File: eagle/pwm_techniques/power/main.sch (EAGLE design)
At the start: 12 parts

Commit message: [ update ] pwm_techniques/power
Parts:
- added C7: 15u, rcl:C-EUC1206
- added L1: 33u, rcl:L-EUTJ3-U2
- added LOAD_CON: (no value), pinhead:PINHD-1X2
- added Q1, Q2, Q3, Q4: IRFP460A, irfp460a:IRFP460A
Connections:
- new net LOAD_N: LOAD_CON.2
- new net LOAD_P: LOAD_CON.1
- new net N$3: L1.2, Q1.SOURCE, Q3.DRAIN
- new net N$4: C7.1, L1.1
- new net N$5: C7.2, Q2.SOURCE, Q4.DRAIN
- net GND: now also Q3.SOURCE, Q4.SOURCE
- net PWR_170V: now also Q1.DRAIN, Q2.DRAIN
- net Q0_GATE: now also Q1.GATE
- net Q1_GATE: now also Q3.GATE
- net Q2_GATE: now also Q2.GATE
- net Q3_GATE: now also Q4.GATE
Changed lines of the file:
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@@
 <part name="C6" library="rcl" deviceset="C-EU" device="C1206" value="100n"/>
 <part name="PWR_CON" library="pinhead" deviceset="PINHD-1X2" device=""/>
+<part name="Q1" library="irfp460a" deviceset="IRFP460A" device=""/>
+<part name="Q2" library="irfp460a" deviceset="IRFP460A" device=""/>
+<part name="Q3" library="irfp460a" deviceset="IRFP460A" device=""/>
+<part name="Q4" library="irfp460a" deviceset="IRFP460A" device=""/>
+<part name="L1" library="rcl" deviceset="L-EU" device="TJ3-U2" value="33u"/>
+<part name="C7" library="rcl" deviceset="C-EU" device="C1206" value="15u"/>
+<part name="LOAD_CON" library="pinhead" deviceset="PINHD-1X2" device=""/>
 </parts>
 <sheets>
@@
 <instance part="C6" gate="G$1" x="-7.62" y="-20.32"/>
 <instance part="PWR_CON" gate="G$1" x="-40.64" y="-5.08"/>
+<instance part="Q1" gate="G$1" x="106.68" y="22.86"/>
+<instance part="Q2" gate="G$1" x="160.02" y="22.86"/>
+<instance part="Q3" gate="G$1" x="106.68" y="-7.62"/>
+<instance part="Q4" gate="G$1" x="160.02" y="-7.62"/>
+<instance part="L1" gate="G$1" x="121.92" y="7.62" rot="R270"/>
+<instance part="C7" gate="G$1" x="134.62" y="7.62" rot="R90"/>
+<instance part="LOAD_CON" gate="G$1" x="-40.64" y="-22.86"/>
 </instances>
 <busses>
@@
 <label x="-68.58" y="-5.08" size="1.778" layer="95"/>
 </segment>
+<segment>
+<pinref part="Q3" gate="G$1" pin="SOURCE"/>
+<wire x1="93.98" y1="-12.7" x2="78.74" y2="-12.7" width="0.1524" layer="91"/>
+<label x="78.74" y="-12.7" size="1.778" layer="95"/>
+</segment>
+<segment>
+<pinref part="Q4" gate="G$1" pin="SOURCE"/>
+<wire x1="147.32" y1="-12.7" x2="127" y2="-12.7" width="0.1524" layer="91"/>
+<label x="127" y="-12.7" size="1.778" layer="95"/>
+</segment>
 </net>
 <net name="PWM_CTL_LO_0" class="0">
@@
 <label x="27.94" y="22.86" size="1.778" layer="95"/>
 </segment>
+<segment>
+<pinref part="Q1" gate="G$1" pin="GATE"/>
+<wire x1="93.98" y1="27.94" x2="78.74" y2="27.94" width="0.1524" layer="91"/>
+<label x="78.74" y="27.94" size="1.778" layer="95"/>
+</segment>
 </net>
 <net name="Q1_GATE" class="0">
@@
 <wire x1="25.4" y1="17.78" x2="38.1" y2="17.78" width="0.1524" layer="91"/>
 <label x="27.94" y="17.78" size="1.778" layer="95"/>
+</segment>
+<segment>
+<pinref part="Q3" gate="G$1" pin="GATE"/>
+<wire x1="93.98" y1="-2.54" x2="78.74" y2="-2.54" width="0.1524" layer="91"/>
+<label x="78.74" y="-2.54" size="1.778" layer="95"/>
 </segment>
 </net>
@@
 <label x="27.94" y="-12.7" size="1.778" layer="95"/>
 </segment>
+<segment>
+<pinref part="Q2" gate="G$1" pin="GATE"/>
+<wire x1="147.32" y1="27.94" x2="132.08" y2="27.94" width="0.1524" layer="91"/>
+<label x="132.08" y="27.94" size="1.778" layer="95"/>
+</segment>
 </net>
 <net name="Q3_GATE" class="0">
@@
 <label x="27.94" y="-17.78" size="1.778" layer="95"/>
 </segment>
+<segment>
+<pinref part="Q4" gate="G$1" pin="GATE"/>
+<wire x1="147.32" y1="-2.54" x2="127" y2="-2.54" width="0.1524" layer="91"/>
+<label x="127" y="-2.54" size="1.778" layer="95"/>
+</segment>
 </net>
 <net name="PWR_170V" class="0">
@@
 <label x="-68.58" y="-2.54" size="1.778" layer="95"/>
 </segment>
-</net>
+<segment>
+<pinref part="Q1" gate="G$1" pin="DRAIN"/>
+<wire x1="93.98" y1="22.86" x2="78.74" y2="22.86" width="0.1524" layer="91"/>
+<label x="78.74" y="22.86" size="1.778" layer="95"/>
+</segment>
+<segment>
+<pinref part="Q2" gate="G$1" pin="DRAIN"/>
+<wire x1="132.08" y1="22.86" x2="147.32" y2="22.86" width="0.1524" layer="91"/>
+<label x="132.08" y="22.86" size="1.778" layer="95"/>
+</segment>
+</net>
+<net name="N$3" class="0">
+<segment>
+<pinref part="Q1" gate="G$1" pin="SOURCE"/>
+<wire x1="93.98" y1="17.78" x2="91.44" y2="17.78" width="0.1524" layer="91"/>
+<wire x1="91.44" y1="17.78" x2="91.44" y2="7.62" width="0.1524" layer="91"/>
+<pinref part="L1" gate="G$1" pin="2"/>
+<wire x1="91.44" y1="7.62" x2="116.84" y2="7.62" width="0.1524" layer="91"/>
+<pinref part="Q3" gate="G$1" pin="DRAIN"/>
+<wire x1="93.98" y1="-7.62" x2="91.44" y2="-7.62" width="0.1524" layer="91"/>
+<wire x1="91.44" y1="-7.62" x2="91.44" y2="7.62" width="0.1524" layer="91"/>
+<junction x="91.44" y="7.62"/>
+</segment>
+</net>
+<net name="N$4" class="0">
+<segment>
+<pinref part="L1" gate="G$1" pin="1"/>
+<pinref part="C7" gate="G$1" pin="1"/>
+<wire x1="127" y1="7.62" x2="132.08" y2="7.62" width="0.1524" layer="91"/>
+</segment>
+</net>
+<net name="N$5" class="0">
+<segment>
+<pinref part="C7" gate="G$1" pin="2"/>
+<wire x1="139.7" y1="7.62" x2="144.78" y2="7.62" width="0.1524" layer="91"/>
+<wire x1="144.78" y1="7.62" x2="144.78" y2="17.78" width="0.1524" layer="91"/>
+<pinref part="Q2" gate="G$1" pin="SOURCE"/>
+<wire x1="144.78" y1="17.78" x2="147.32" y2="17.78" width="0.1524" layer="91"/>
+<pinref part="Q4" gate="G$1" pin="DRAIN"/>
+<wire x1="147.32" y1="-7.62" x2="144.78" y2="-7.62" width="0.1524" layer="91"/>
+<wire x1="144.78" y1="-7.62" x2="144.78" y2="7.62" width="0.1524" layer="91"/>
+<junction x="144.78" y="7.62"/>
+</segment>
+</net>
+<net name="LOAD_P" class="0">
+<segment>
+<pinref part="LOAD_CON" gate="G$1" pin="1"/>
+<wire x1="-43.18" y1="-20.32" x2="-68.58" y2="-20.32" width="0.1524" layer="91"/>
+<label x="-68.58" y="-20.32" size="1.778" layer="95"/>
+</segment>
+</net>
+<net name="LOAD_N" class="0">
+<segment>
+<pinref part="LOAD_CON" gate="G$1" pin="2"/>
+<wire x1="-43.18" y1="-22.86" x2="-68.58" y2="-22.86" width="0.1524" layer="91"/>
+<label x="-68.58" y="-22.86" size="1.778" layer="95"/>
+</segment>
+</net>

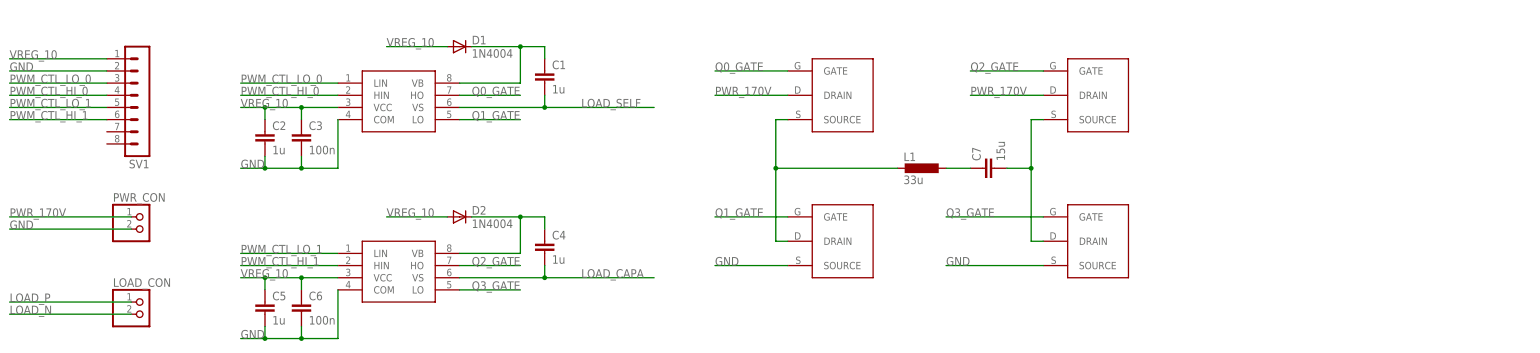
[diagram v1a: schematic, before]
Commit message: [ update ] add pwm exclusion logic
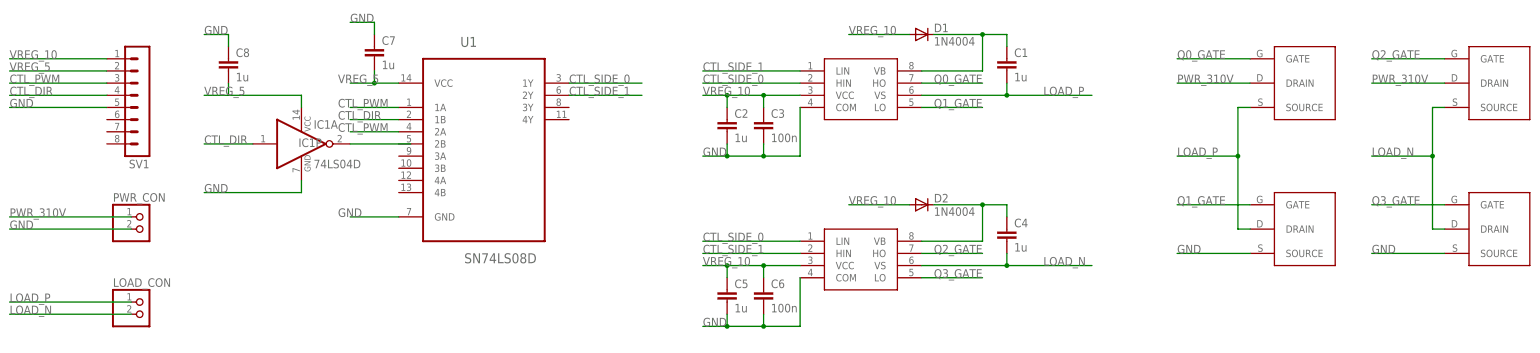
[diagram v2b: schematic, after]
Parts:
- removed L1: 33u, rcl:L-EUTJ3-U2
- added C8: 1u, rcl:C-EUC1206
- added IC1: 74LS04D, 74xx-eu:74LS04D
- added U1: SN74LS08D, sn74ls08d:SN74LS08D
- C7: value 15u -> 1u
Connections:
- net PWR_170V renamed PWR_310V
- removed net LOAD_CAPA: C4.2, IR2304_1.VS
- removed net LOAD_SELF: C1.2, IR2304_0.VS
- removed net N$3: L1.2, Q1.SOURCE, Q3.DRAIN
- removed net N$4: C7.1, L1.1
- removed net PWM_CTL_HI_0: IR2304_0.HIN, SV1.4
- removed net PWM_CTL_HI_1: IR2304_1.HIN, SV1.6
- removed net PWM_CTL_LO_0: IR2304_0.LIN, SV1.3
- removed net PWM_CTL_LO_1: IR2304_1.LIN, SV1.5
- new net CTL_DIR: IC1A.I, SV1.4, U1.1B
- new net CTL_PWM: SV1.3, U1.1A, U1.2A
- new net CTL_SIDE_0: IR2304_0.HIN, IR2304_1.LIN, U1.1Y
- new net CTL_SIDE_1: IR2304_0.LIN, IR2304_1.HIN, U1.2Y
- new net VREG_1: C8.2
- new net VREG_5: C7.2, IC1P.VCC, SV1.2, U1.VCC
- net GND: now also C7.1, C8.1, IC1P.GND, SV1.5, U1.GND; no longer SV1.2
- net LOAD_N: now also C4.2, IR2304_1.VS, Q2.SOURCE, Q4.DRAIN
- net LOAD_P: now also C1.2, IR2304_0.VS, Q1.SOURCE, Q3.DRAIN
- net N$5: now also IC1A.O; no longer C7.2, Q2.SOURCE, Q4.DRAIN
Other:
- moved on the sheet: C1, C2, C3, C4, C5, C6, C7, D1, D2
